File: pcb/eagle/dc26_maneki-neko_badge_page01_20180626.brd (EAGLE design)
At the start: 75.8 x 126.7 mm, 55 parts, among them T1 RK7002BMT116, U1 STM32F030C8T, U2 PAM2301CAAB330, U3 NPTC042KFMS-RC, U4 MIC2005A-1YM5-TR, U5 MIC2005A-1YM5-TR, U6 MIC2005A-1YM5-TR

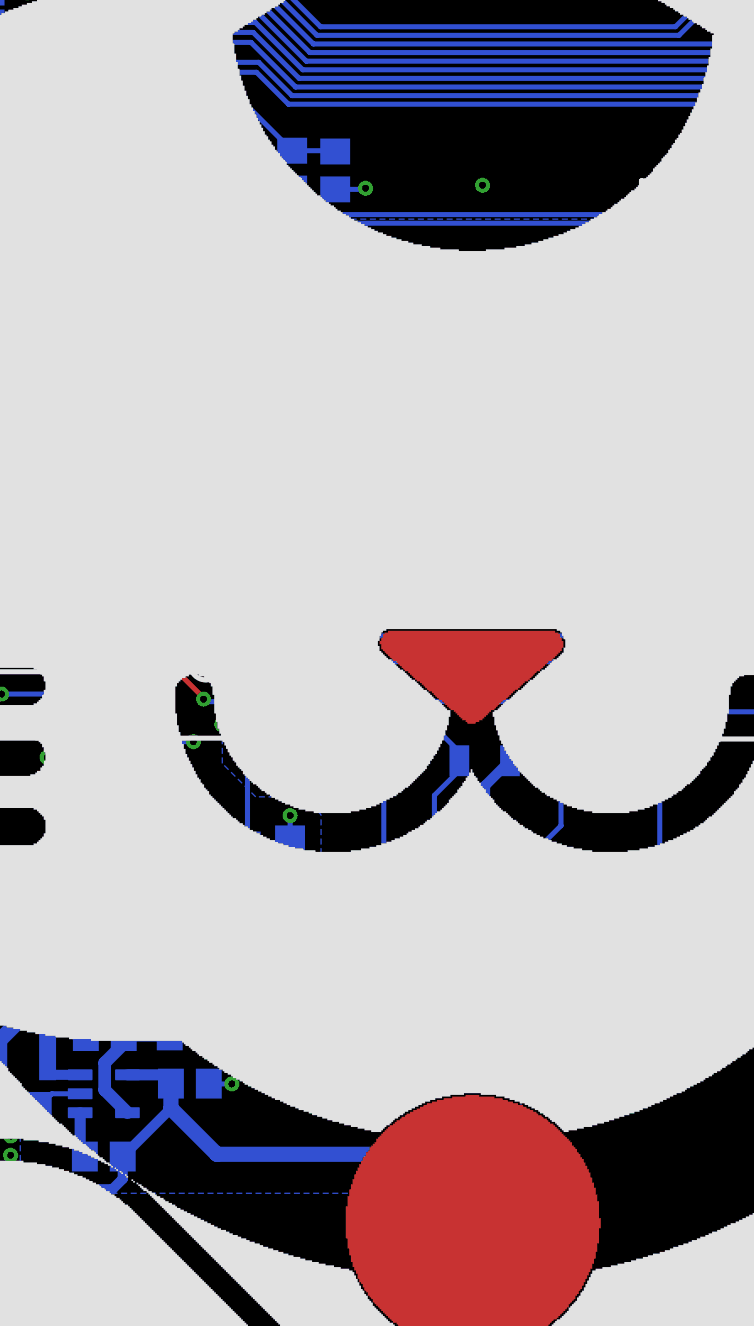
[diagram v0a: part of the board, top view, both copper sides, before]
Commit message: added power switch and user button
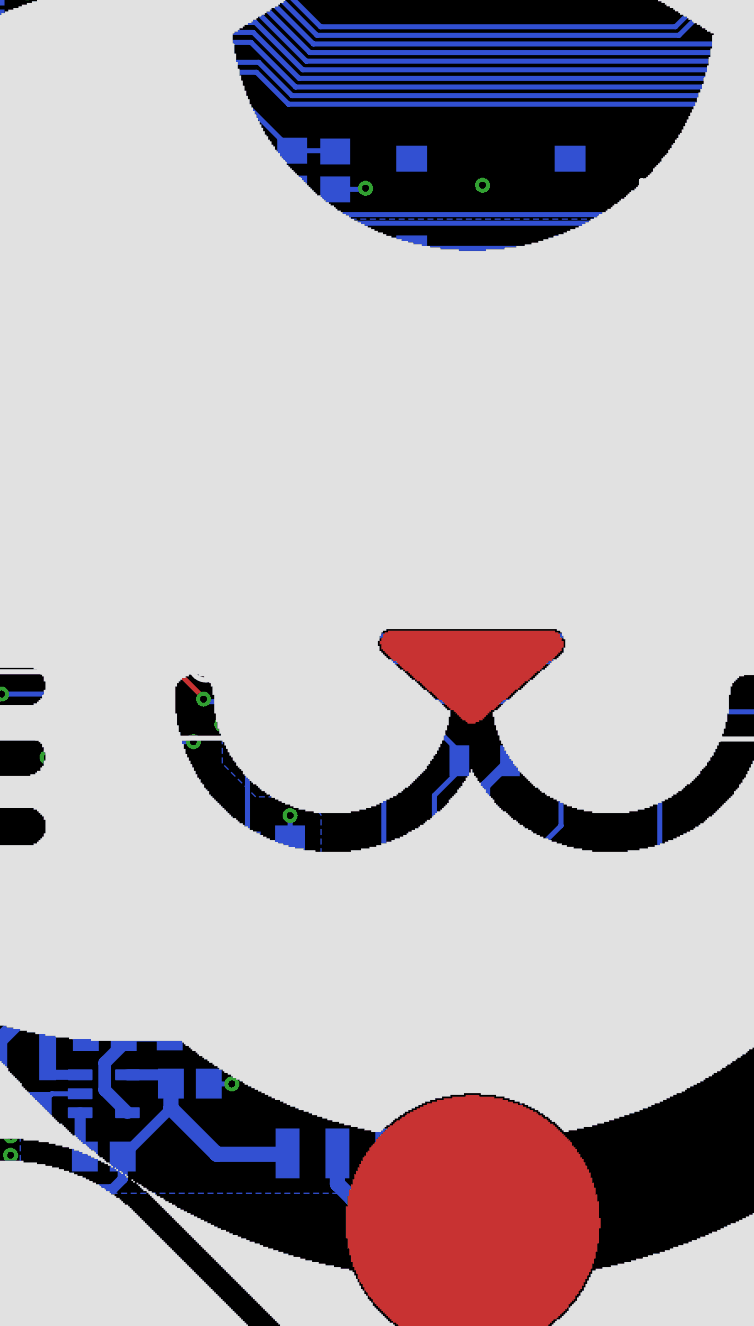
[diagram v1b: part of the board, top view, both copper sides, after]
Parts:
- removed U$1: BATTPADS-SMT, battery_pads:BATTPADS-SMT
- added S1: JS202011SCQN, JS202011SCQN:SW_JS202011SCQN
- added SW1: PTS645SM43SMTR92, PTS645SM43SMTR92:PTS645SM43SMTR92
- added U$2: BATTPADS-SMT, battery_pads:BATTPADS-SMT
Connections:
- new net USER_BUTTON: SW1.3, SW1.4, U1.2
- new net VBATIN: S1.2, U$2.1
- net GND: now also SW1.1, SW1.2, U$2.2; no longer U$1.2
- net VBAT: now also S1.3; no longer U$1.1
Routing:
- net USER_BUTTON: track 0.00 -> 27.1 mm, vias 0 -> 2
- net VBATIN: track 0.00 -> 10.2 mm
- net VBAT: track 58.4 -> 50.3 mm
- net GND: track 118.3 -> 112.7 mm, vias 28 -> 25

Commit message: OUT TO FAB OMG 2560256025602560
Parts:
- moved H1 7.12 mm to (63.6, 111.6)
- moved C6 7.12 mm to (61.6, 114.1)
- moved H3 6.00 mm to (38.0, 18.2), turned to 45 degrees
- moved R27 1.40 mm to (18.3, 117.8), turned to 180 degrees
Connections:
- net !RESET: now also H1.9; no longer H1.10
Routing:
- net GND: track 112.7 -> 118.3 mm, vias 25 -> 23
- net I2C1_SCL: track 142.8 -> 139.0 mm
- net SWDIO: track 46.8 -> 44.1 mm
- net SWCLK: track 41.7 -> 39.0 mm
- net I2C1_SDA: track 137.5 -> 140.1 mm
- net 3V3: track 78.0 -> 80.3 mm
- net !RESET: track 51.9 -> 52.6 mm
- net VBATIN: track 10.2 -> 9.51 mm
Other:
- board text added: "&"
- board text added: "dash"
- board text added: "dc26"
- board text added: "github.com/SeanLeftBelow/defcon26-meow"
- board text added: "tense future"
